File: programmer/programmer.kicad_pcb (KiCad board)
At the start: 2 copper layers, 52.1 x 20.3 mm, 2 parts

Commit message: Hmmmm
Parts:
- added C1: 10uF, Capacitor_SMD:C_0805_2012Metric, F.Cu at (201.9, 104.1)
- added C2: 10uF, Capacitor_SMD:C_0805_2012Metric, F.Cu at (191.8, 104.1)
- added J1: ~, Connector_PinHeader_2.54mm:PinHeader_2x03_P2.54mm_Horizontal, F.Cu at (155.6, 104.1)
- added U1: AMS1117-3.3, Package_TO_SOT_SMD:SOT-223-3_TabPin2, F.Cu at (196.8, 102.2)
- J3, J4: footprint Connector_PinHeader_2.54mm:PinHeader_1x20_P2.54mm_Vertical -> Connector_PinSocket_2.54mm:PinSocket_1x20_P2.54mm_Vertical; moved to F.Cu
- turned J3 to 90 degrees
- turned J4 to 90 degrees
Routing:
- net B14: track 0.00 -> 47.9 mm
- net B13: track 0.00 -> 47.0 mm
- net +3V3: track 0.00 -> 45.8 mm, vias 0 -> 15
- net +5V: track 0.00 -> 7.32 mm
- added copper zone on B.Cu, net +3V3
- added copper zone on F.Cu, net +3V3
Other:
- board text added: "Green Pill Programmer, rev. c STM32 Programmer © 2020 Lars Boegild Thomsen"
- board text removed: "Green Pill, rev. c STM32 Development Board © 2020 Lars Boegild Thomsen"

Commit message: Hmmm
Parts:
- added R1: 100, Resistor_SMD:R_0603_1608Metric, F.Cu at (187.3, 97.8)
- added R2: 4.7, Resistor_SMD:R_0603_1608Metric, F.Cu at (163.8, 104.8)
- added R3: 4.7, Resistor_SMD:R_0603_1608Metric, F.Cu at (165.7, 104.8)
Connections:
- J1 pad 6: Net-(J1-Pad6) -> A10
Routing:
- net A10: track 0.00 -> 36.1 mm
- net B12: track 0.00 -> 16.5 mm
- net A0: track 0.00 -> 5.53 mm
- net +3V3: track 45.8 -> 48.3 mm

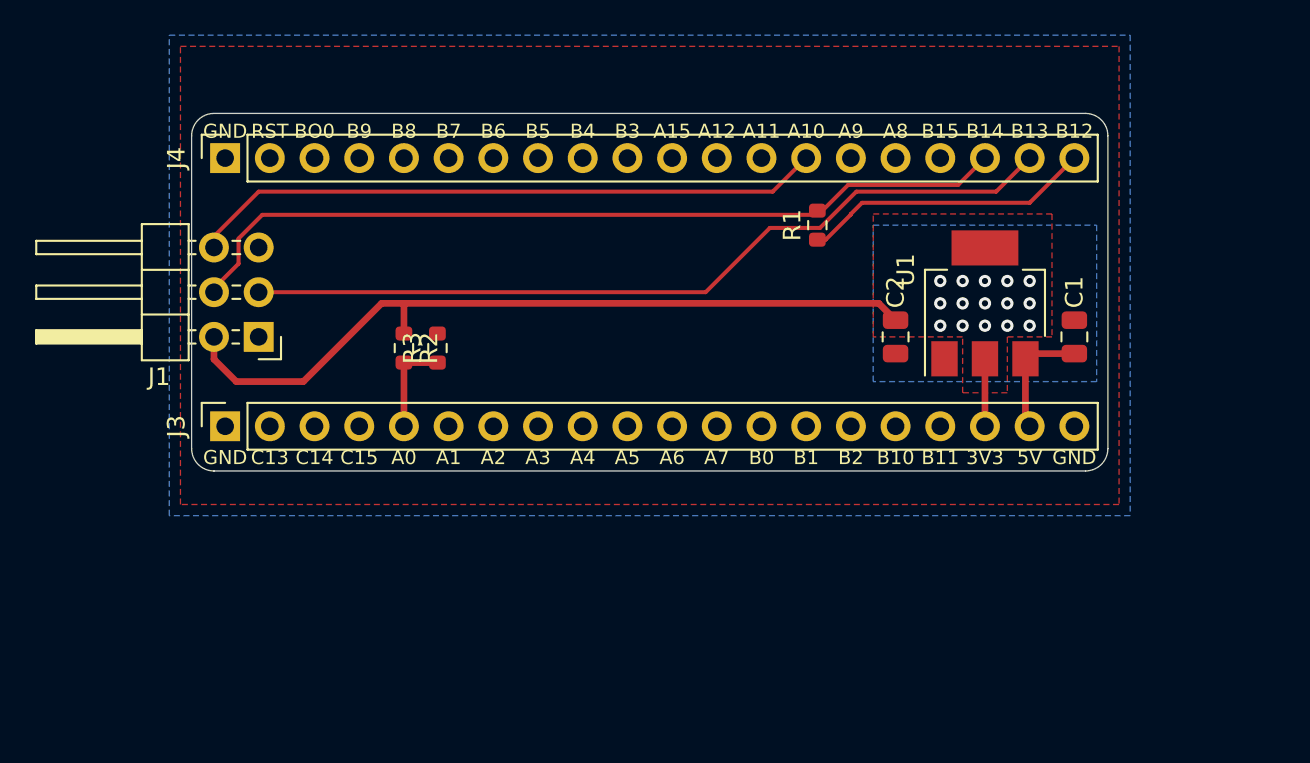
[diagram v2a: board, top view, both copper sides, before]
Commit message: Added headers
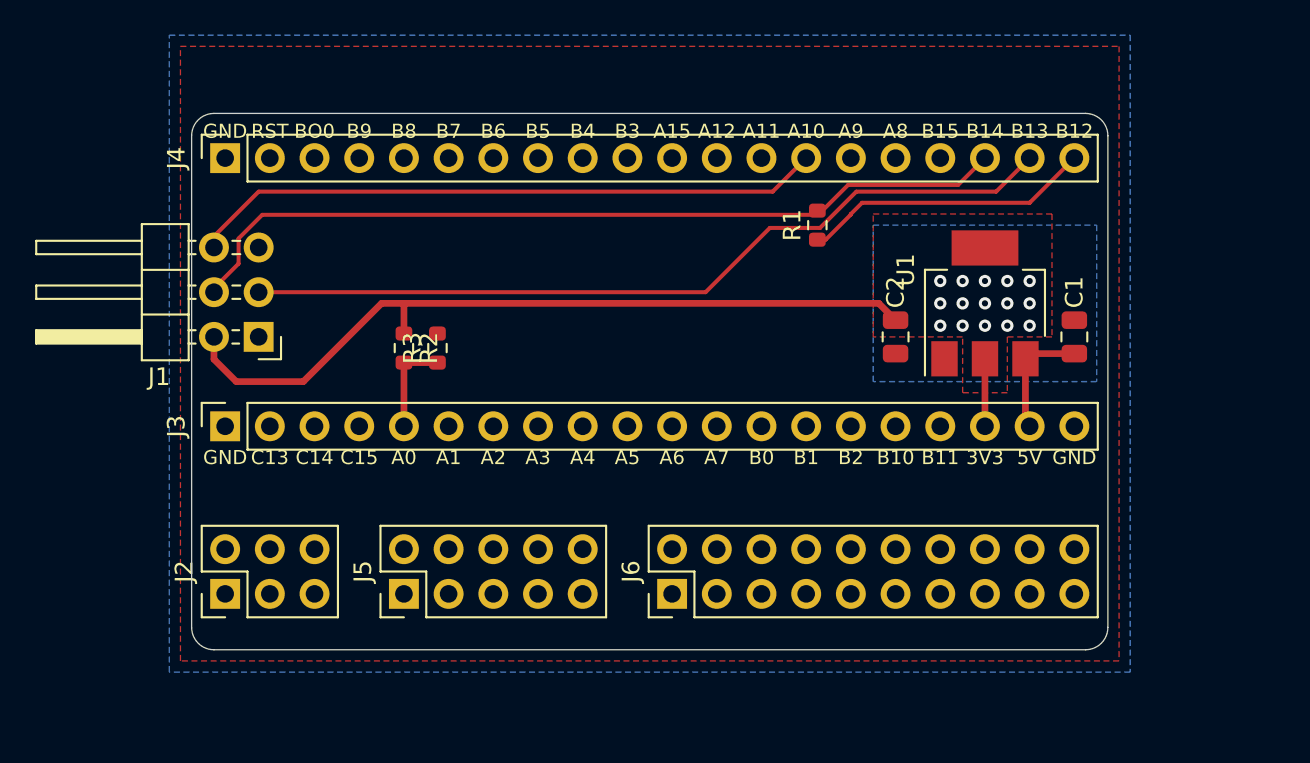
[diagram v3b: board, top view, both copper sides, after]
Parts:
- added J2: ~, Connector_PinHeader_2.54mm:PinHeader_2x03_P2.54mm_Vertical, F.Cu at (153.7, 118.7)
- added J5: ~, Connector_PinHeader_2.54mm:PinHeader_2x05_P2.54mm_Vertical, F.Cu at (163.8, 118.7)
- added J6: ~, Connector_PinHeader_2.54mm:PinHeader_2x10_P2.54mm_Vertical, F.Cu at (179.1, 118.7)
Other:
- board size 52.1 x 20.3 mm -> 52.1 x 30.5 mm

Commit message: Hmmmm
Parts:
- added D1: YL, LED_SMD:LED_0603_1608Metric, F.Cu at (208.9, 113.7)
- added D2: GR, LED_SMD:LED_0603_1608Metric, F.Cu at (212.1, 104.8)
- added D3: BL, LED_SMD:LED_0603_1608Metric, F.Cu at (209.6, 108.6)
- added D4: RD, LED_SMD:LED_0603_1608Metric, F.Cu at (212.1, 100.3)
- added D5: RD, LED_SMD:LED_0603_1608Metric, F.Cu at (199.4, 116.2)
- added D6: BL, LED_SMD:LED_0603_1608Metric, F.Cu at (202.6, 116.2)
- added NT1: ~, NetTie:NetTie-2_THT_Pad0.3mm, F.Cu at (183.5, 96.5)
- added R4: 470, Resistor_SMD:R_0603_1608Metric, F.Cu at (199.4, 113.0)
- added R5: 470, Resistor_SMD:R_0603_1608Metric, F.Cu at (202.6, 113.0)
- moved J2 3.81 mm to (153.7, 122.6)
- moved J5 3.81 mm to (163.8, 122.6)
- moved J6 3.81 mm to (179.1, 122.6)
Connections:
- J1 pad 6: A10 -> T_SWO
- J2 pad 2: Net-(J2-Pad2) -> +3V3
- J2 pad 3: Net-(J2-Pad3) -> B13
- J2 pad 4: Net-(J2-Pad4) -> B14
- J2 pad 5: Net-(J2-Pad5) -> GND
- J2 pad 6: Net-(J2-Pad6) -> T_SWO
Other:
- board size 52.1 x 30.5 mm -> 52.1 x 33.7 mm
